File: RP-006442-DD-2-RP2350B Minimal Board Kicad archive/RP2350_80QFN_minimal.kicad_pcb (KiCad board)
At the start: 2 copper layers, 99.4 x 99.4 mm, 167 parts, among them J1 USB_C_Receptacle_USB2.0_16P, J2 Conn_02x14_Odd_Even, J3 Conn_02x09_Odd_Even, J4 Conn_01x03, J5 USB_C_Receptacle_USB2.0_16P, J6 Conn_01x05, SW1 SW_Push, SW10 SW_DIP_x08, SW2 SW_Push, SW3 SW_Push, SW4 SW_Push, SW5 SW_Push, SW6 SW_Push, SW7 SW_Push, SW8 SW_Push, SW9 SW_SPDT, U1 RP2350_80QFN, U10 74HC595, U11 74HC595, U12 74HC595, U13 MMA8451QR1, U14 GS3011CR-G, U15 GS3011CR-G, U16 GS3011CR-G, U17 GS3011CR-G, U2 NCP1117-3.3_SOT223, U3 W25Q128JVS, U4 DNF, U5 W25Q128JVS, U6 NCP1117-3.3_SOT223, U7 RP2350_60QFN, U8 HT16K33A-24SSOP, U9 CC56-12EWA, Y1 ABM8-272-T3, Y2 ABM8-272-T3

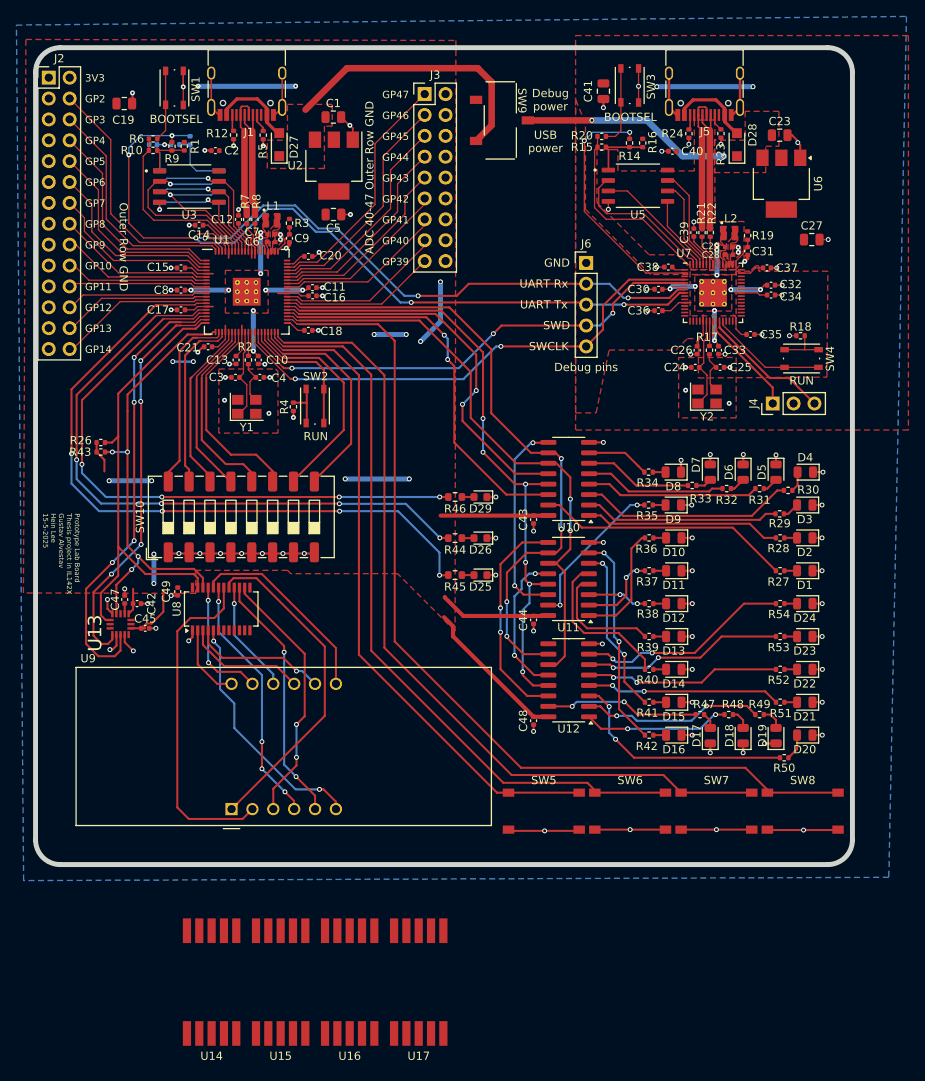
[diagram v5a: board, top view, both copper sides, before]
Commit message: Update hex display pcb traces
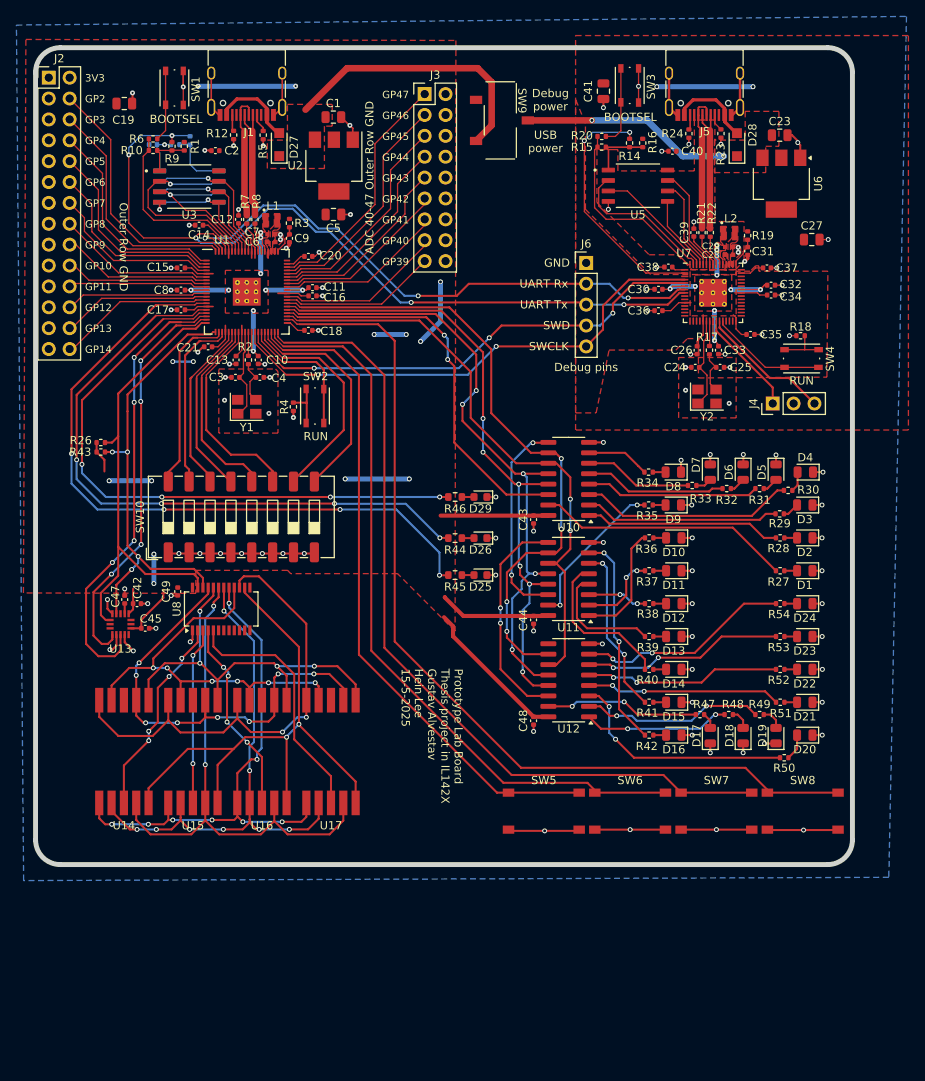
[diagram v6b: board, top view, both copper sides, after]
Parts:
- removed U9: CC56-12EWA, Display_7Segment:CA56-12EWA
- moved U17 30.0 mm to (98.1, 131.0)
- moved U14 30.0 mm to (72.9, 131.0)
- moved U15 30.0 mm to (81.3, 131.0)
- moved U16 30.0 mm to (89.7, 131.0)
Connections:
- net /VSYS renamed /VSYS_A
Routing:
- net /Hex displays peripheral/ROW0: track 15.6 -> 54.7 mm, vias 2 -> 8
- net /Hex displays peripheral/ROW7: track 31.6 -> 70.5 mm
- net /Hex displays peripheral/ROW5: track 13.7 -> 50.9 mm, vias 1 -> 6
- net /Hex displays peripheral/ROW2: track 30.8 -> 64.8 mm, vias 4 -> 2
- net /Hex displays peripheral/ROW6: track 30.8 -> 59.4 mm
- net /Hex displays peripheral/ROW1: track 24.1 -> 50.2 mm, vias 0 -> 4
- net /Hex displays peripheral/ROW4: track 40.4 -> 63.2 mm, vias 0 -> 8
- net /Hex displays peripheral/ROW3: track 41.0 -> 63.7 mm, vias 0 -> 8
- net /Hex displays peripheral/COM0: track 9.23 -> 24.7 mm, vias 0 -> 4
- net /GPIO36: track 65.3 -> 78.0 mm, vias 4 -> 5
- net /Hex displays peripheral/COM2: track 16.7 -> 23.8 mm, vias 1 -> 4
- net /Hex displays peripheral/COM1: track 14.8 -> 21.5 mm, vias 0 -> 2
- net /Hex displays peripheral/COM3: track 29.9 -> 30.7 mm, vias 2 -> 0
- net +3V3_A: track 146.3 -> 145.7 mm, vias 1 -> 15
- net +3V3: vias 16 -> 2
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- added copper zone on F.Cu, net +1V1_A
- added copper zone on F.Cu, net +3V3_A

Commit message: Update
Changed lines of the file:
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@@
 		(polygon
 			(pts
-				(xy 60.975 44.35) (xy 113.3 44.475) (xy 113.199715 116.35) (xy 106.20145 109.35) (xy 93.2 109.35)
-				(xy 92.824238 108.95) (xy 81.65 108.95) (xy 81.65 111.751877) (xy 60.675 111.7)
+				(xy 60.975 44.35) (xy 113.3 44.475) (xy 113.199715 116.35) (xy 106.2 108.95) (xy 81.65 108.95) (xy 81.65 111.751877)
+				(xy 60.675 111.7)
 			)
 		)

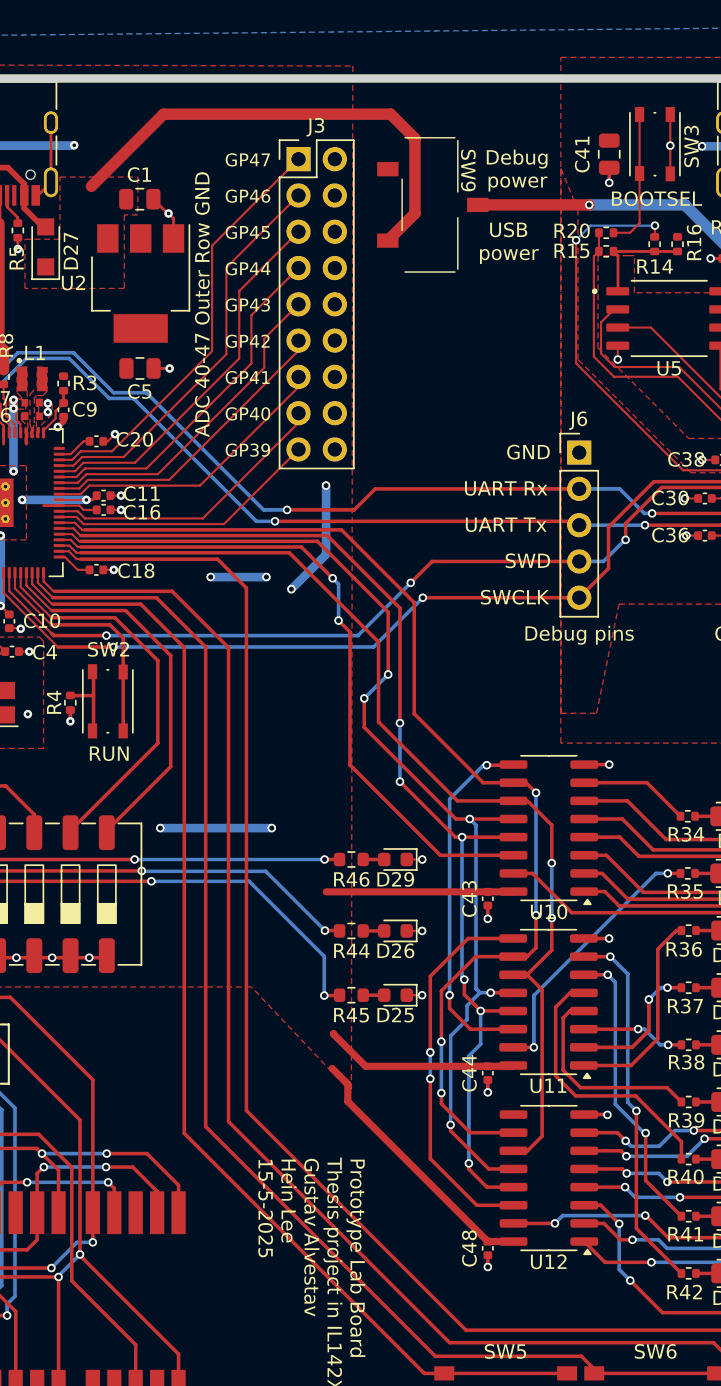
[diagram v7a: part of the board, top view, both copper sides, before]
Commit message: Update usb power switch
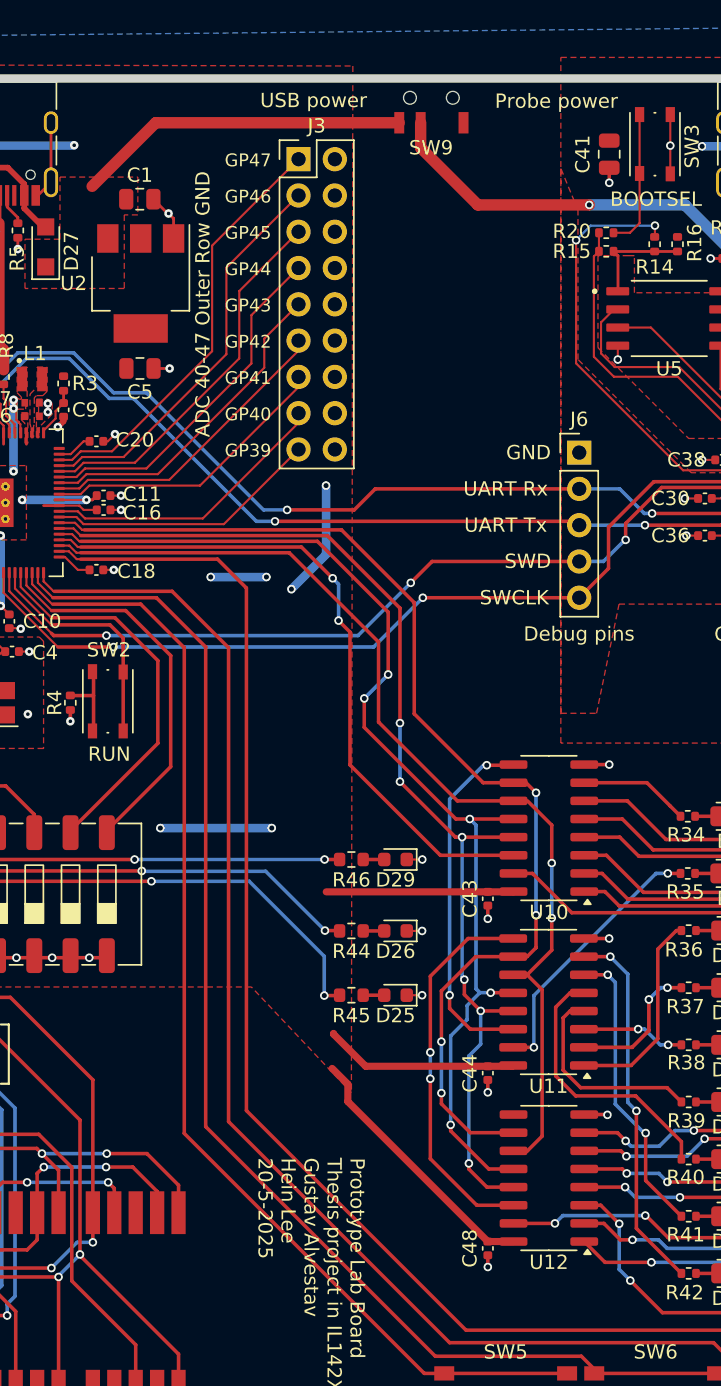
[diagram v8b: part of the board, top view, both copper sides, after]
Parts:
- SW9: footprint Button_Switch_SMD:SW_SPDT_HRO_K3-1235S-K1 -> Button_Switch_SMD:SW_SPDT_G-Switch_MK-12C03-G015
- moved SW9 5.86 mm to (118.8, 46.7), turned to 180 degrees
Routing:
- net /VSYS_A: track 59.0 -> 56.4 mm
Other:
- board text added: "Probe power"
- board text added: "Prototype Lab Board Thesis project in IL142X Gustav Alvestav Hein Lee 20-5-2025"
- board text removed: "Debug power"
- board text removed: "Prototype Lab Board Thesis project in IL142X Gustav Alvestav Hein Lee 15-5-2025"
